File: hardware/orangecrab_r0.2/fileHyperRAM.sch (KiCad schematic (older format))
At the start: 33 parts, among them U4 MT41K64M16TW-107_J-TR

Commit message: hw: Update I/O block routing new DDR3 signals.
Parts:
- gave numbers to parts that had none: 1
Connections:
- net RAM_D0: now also U4.E3 (DQ0); no longer U4.D7 (DQ8)
- net RAM_D1: now also U4.F7 (DQ1); no longer U4.C3 (DQ9)
- net RAM_D10: now also U4.C8 (DQ10); no longer U4.F2 (DQ2)
- net RAM_D11: now also U4.C2 (DQ11); no longer U4.F8 (DQ3)
- net RAM_D12: now also U4.A7 (DQ12); no longer U4.H3 (DQ4)
- net RAM_D13: now also U4.A2 (DQ13); no longer U4.H8 (DQ5)
- net RAM_D14: now also U4.B8 (DQ14); no longer U4.G2 (DQ6)
- net RAM_D15: now also U4.A3 (DQ15); no longer U4.H7 (DQ7)
- net RAM_D2: now also U4.F2 (DQ2); no longer U4.C8 (DQ10)
- net RAM_D3: now also U4.F8 (DQ3); no longer U4.C2 (DQ11)
- net RAM_D4: now also U4.H3 (DQ4); no longer U4.A7 (DQ12)
- net RAM_D5: now also U4.H8 (DQ5); no longer U4.A2 (DQ13)
- net RAM_D6: now also U4.G2 (DQ6); no longer U4.B8 (DQ14)
- net RAM_D7: now also U4.H7 (DQ7); no longer U4.A3 (DQ15)
- net RAM_D8: now also U4.D7 (DQ8); no longer U4.E3 (DQ0)
- net RAM_D9: now also U4.C3 (DQ9); no longer U4.F7 (DQ1)
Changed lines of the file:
@@
 Text GLabel 7050 4100 0    50   Input ~ 0
 RAM_A12
+Text GLabel 8400 3750 2    50   Input ~ 0
+RAM_D0
+Text GLabel 8400 3850 2    50   Input ~ 0
+RAM_D1
+Text GLabel 8400 3950 2    50   Input ~ 0
+RAM_D2
+Text GLabel 8400 4050 2    50   Input ~ 0
+RAM_D3
+Text GLabel 8400 4150 2    50   Input ~ 0
+RAM_D4
+Text GLabel 8400 4250 2    50   Input ~ 0
+RAM_D5
+Text GLabel 8400 4350 2    50   Input ~ 0
+RAM_D6
+Text GLabel 8400 4450 2    50   Input ~ 0
+RAM_D7
 Text GLabel 8400 4650 2    50   Input ~ 0
-RAM_D0
+RAM_D8
 Text GLabel 8400 4750 2    50   Input ~ 0
-RAM_D1
+RAM_D9
 Text GLabel 8400 4850 2    50   Input ~ 0
-RAM_D2
+RAM_D10
 Text GLabel 8400 4950 2    50   Input ~ 0
-RAM_D3
+RAM_D11
 Text GLabel 8400 5050 2    50   Input ~ 0
-RAM_D4
+RAM_D12
 Text GLabel 8400 5150 2    50   Input ~ 0
-RAM_D5
+RAM_D13
 Text GLabel 8400 5250 2    50   Input ~ 0
-RAM_D6
+RAM_D14
 Text GLabel 8400 5350 2    50   Input ~ 0
-RAM_D7
-Text GLabel 8400 3750 2    50   Input ~ 0
-RAM_D8
-Text GLabel 8400 3850 2    50   Input ~ 0
-RAM_D9
-Text GLabel 8400 3950 2    50   Input ~ 0
-RAM_D10
-Text GLabel 8400 4050 2    50   Input ~ 0
-RAM_D11
-Text GLabel 8400 4150 2    50   Input ~ 0
-RAM_D12
-Text GLabel 8400 4250 2    50   Input ~ 0
-RAM_D13
-Text GLabel 8400 4350 2    50   Input ~ 0
-RAM_D14
-Text GLabel 8400 4450 2    50   Input ~ 0
 RAM_D15
 Text GLabel 8400 6000 2    50   Input ~ 0
@@
 RAM_A14
 $Comp
-L Device:R_Pack04 RN?
+L Device:R_Pack04 RN8
 U 1 1 5DE28326
 P 2650 4800
-F 0 "RN?" V 2350 4700 50  0000 C CNN
+F 0 "RN8" V 2350 4700 50  0000 C CNN
 F 1 "50R" V 2350 4950 50  0000 C CNN
 F 2 "Resistor_SMD:R_Array_Convex_4x0402" V 2925 4800 50  0001 C CNN

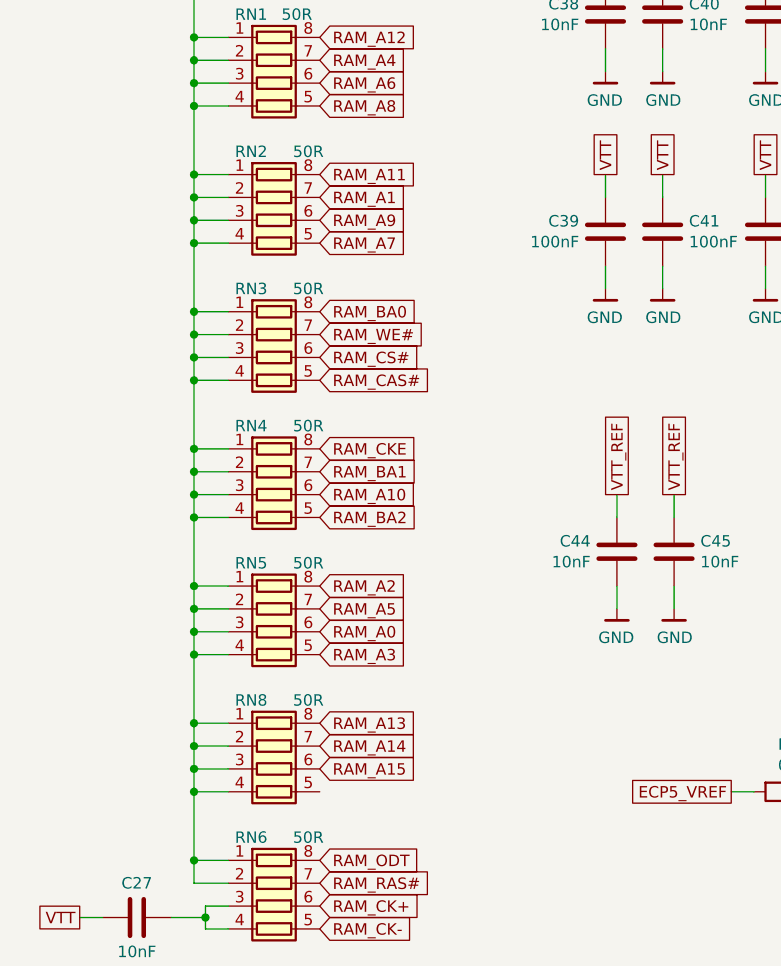
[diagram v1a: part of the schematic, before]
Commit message: hw: update DDR3 signals
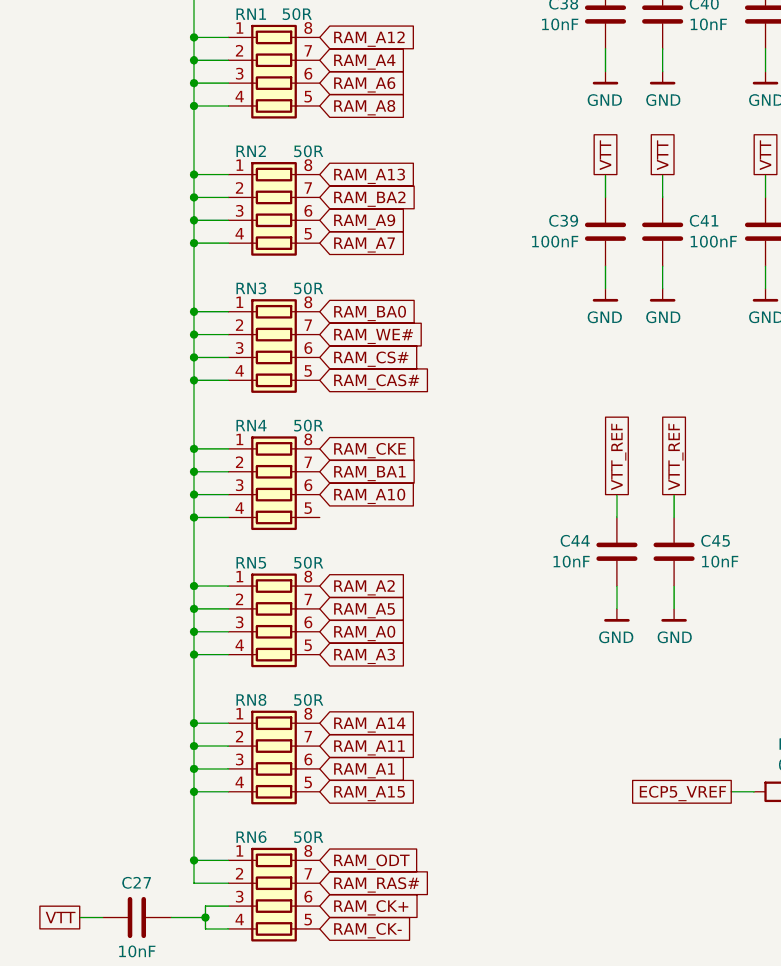
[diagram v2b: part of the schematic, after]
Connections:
- net RAM_A1: now also RN8.6 (R3.2); no longer RN2.7 (R2.2)
- net RAM_A11: now also RN8.7 (R2.2); no longer RN2.8 (R1.2)
- net RAM_A13: now also RN2.8 (R1.2); no longer RN8.8 (R1.2)
- net RAM_A14: now also RN8.8 (R1.2); no longer RN8.7 (R2.2)
- net RAM_A15: now also RN8.5 (R4.2); no longer RN8.6 (R3.2)
- net RAM_BA2: now also RN2.7 (R2.2); no longer RN4.5 (R4.2)
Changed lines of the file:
@@
 Text GLabel 2850 4200 2    50   Input ~ 0
 RAM_A0
-Text GLabel 2850 2300 2    50   Input ~ 0
+Text GLabel 2850 4800 2    50   Input ~ 0
 RAM_A1
 Text GLabel 2850 4000 2    50   Input ~ 0
@@
 Text GLabel 2850 3600 2    50   Input ~ 0
 RAM_A10
-Text GLabel 2850 2200 2    50   Input ~ 0
+Text GLabel 2850 4700 2    50   Input ~ 0
 RAM_A11
 Text GLabel 2850 1600 2    50   Input ~ 0
@@
 Text GLabel 7050 4600 0    50   Input ~ 0
 RAM_BA0
-Text GLabel 2850 3700 2    50   Input ~ 0
+Text GLabel 2850 2300 2    50   Input ~ 0
 RAM_BA2
 Text GLabel 2850 3500 2    50   Input ~ 0
@@
 Text GLabel 7050 4400 0    50   Input ~ 0
 RAM_A15
-Text GLabel 2850 4800 2    50   Input ~ 0
+Text GLabel 2850 4900 2    50   Input ~ 0
 RAM_A15
+Text GLabel 2850 2200 2    50   Input ~ 0
+RAM_A13
 Text GLabel 2850 4600 2    50   Input ~ 0
-RAM_A13
-Text GLabel 2850 4700 2    50   Input ~ 0
 RAM_A14
 $Comp

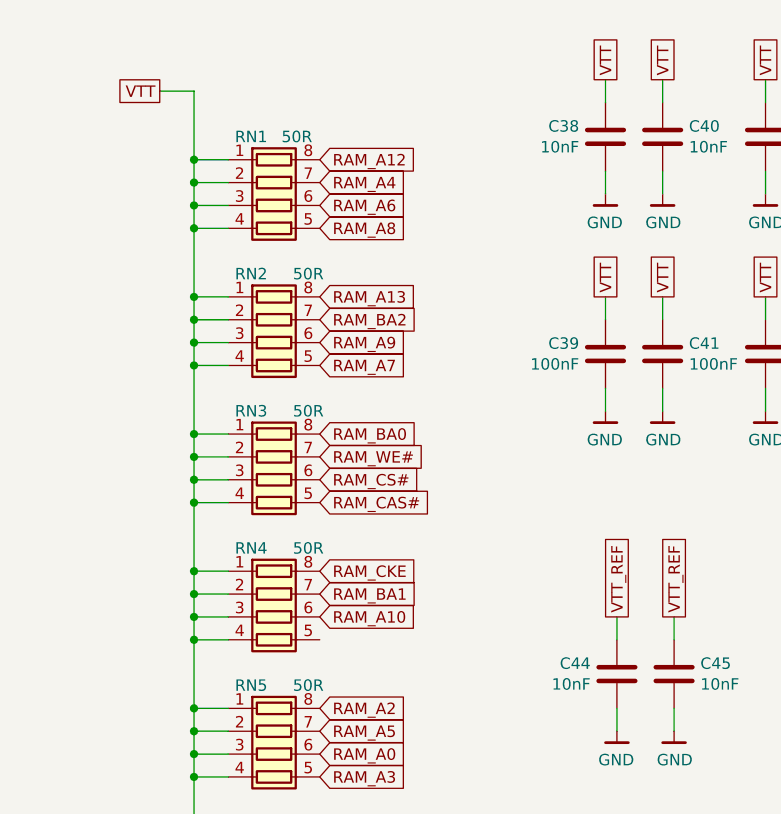
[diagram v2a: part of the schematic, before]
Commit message: hw: Completed first pass of new DD3 routing.
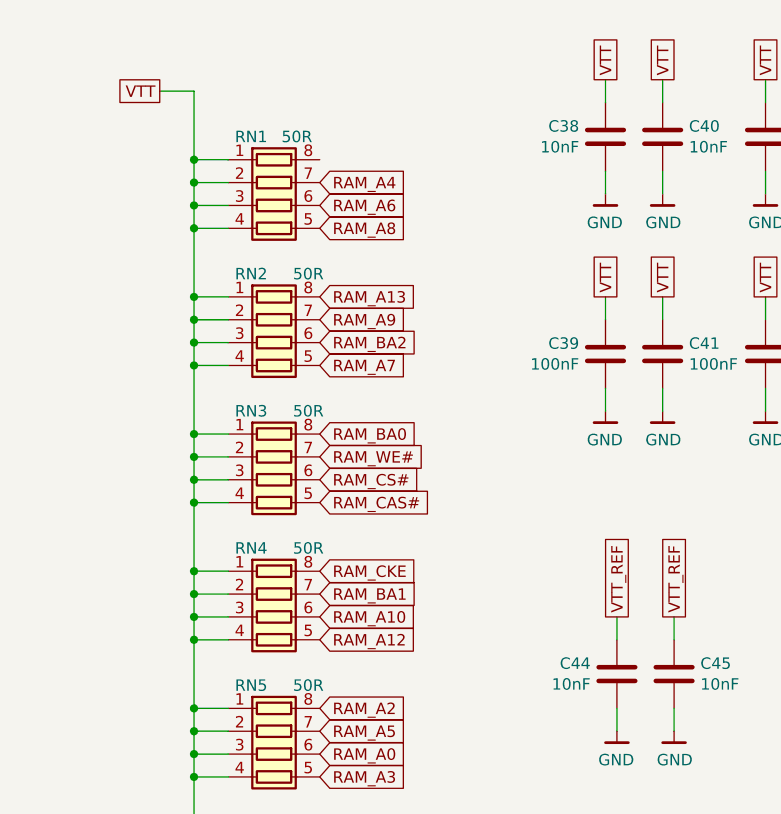
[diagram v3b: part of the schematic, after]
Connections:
- net RAM_A12: now also RN4.5 (R4.2); no longer RN1.8 (R1.2)
- net RAM_A9: now also RN2.7 (R2.2); no longer RN2.6 (R3.2)
- net RAM_BA2: now also RN2.6 (R3.2); no longer RN2.7 (R2.2)
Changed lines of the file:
@@
 Text GLabel 2850 1900 2    50   Input ~ 0
 RAM_A8
-Text GLabel 2850 2400 2    50   Input ~ 0
+Text GLabel 2850 2300 2    50   Input ~ 0
 RAM_A9
 Text GLabel 2850 3600 2    50   Input ~ 0
@@
 Text GLabel 2850 4700 2    50   Input ~ 0
 RAM_A11
-Text GLabel 2850 1600 2    50   Input ~ 0
+Text GLabel 2850 3700 2    50   Input ~ 0
 RAM_A12
 Text GLabel 10450 1950 2    50   UnSpc ~ 0
@@
 Text GLabel 7050 4600 0    50   Input ~ 0
 RAM_BA0
-Text GLabel 2850 2300 2    50   Input ~ 0
+Text GLabel 2850 2400 2    50   Input ~ 0
 RAM_BA2
 Text GLabel 2850 3500 2    50   Input ~ 0

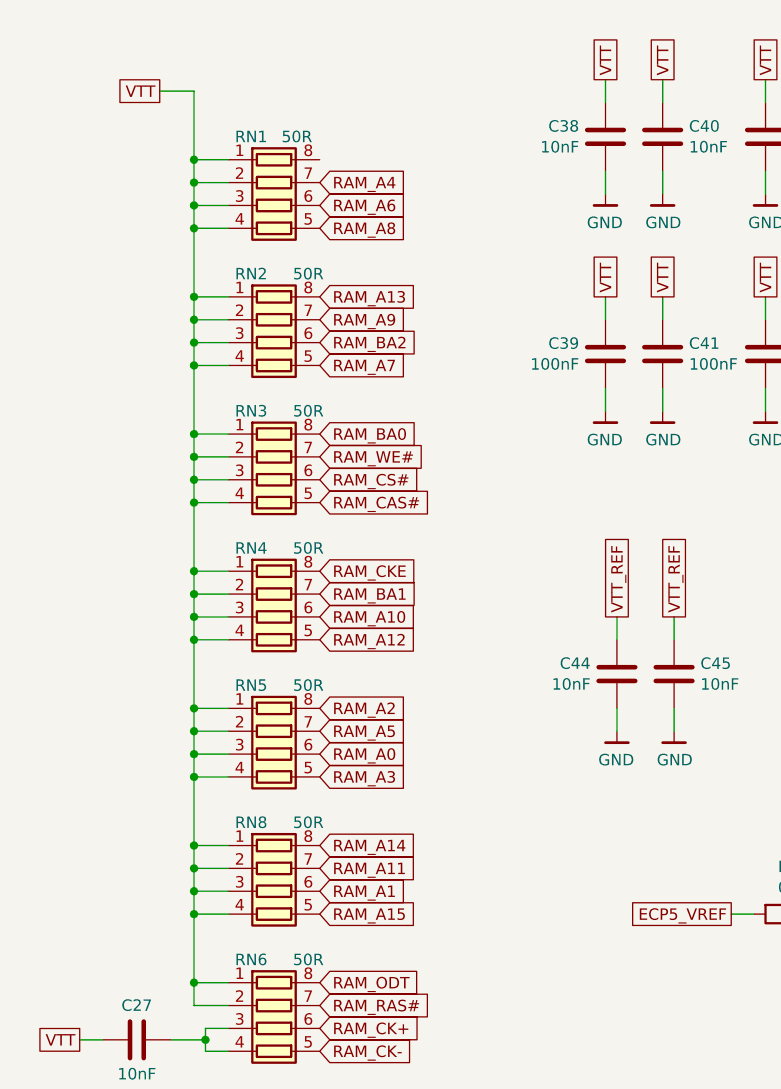
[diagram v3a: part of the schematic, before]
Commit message: hw: Update microSD card
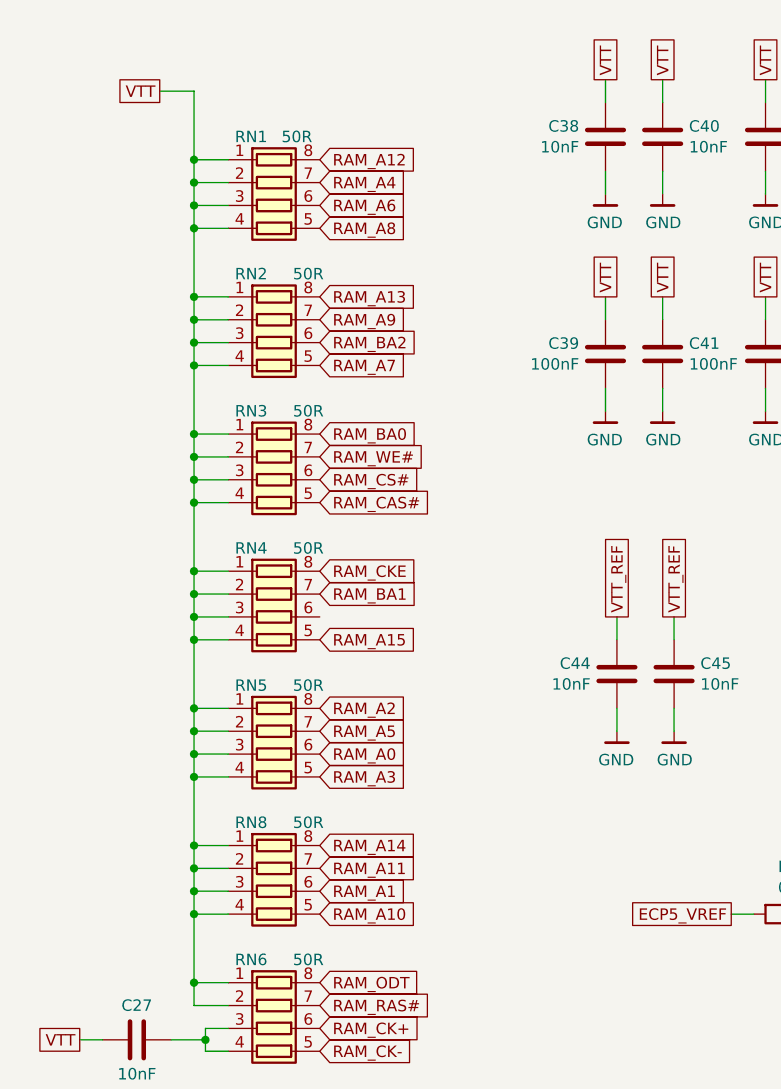
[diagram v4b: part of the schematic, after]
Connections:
- net RAM_A10: now also RN8.5 (R4.2); no longer RN4.6 (R3.2)
- net RAM_A12: now also RN1.8 (R1.2); no longer RN4.5 (R4.2)
- net RAM_A15: now also RN4.5 (R4.2); no longer RN8.5 (R4.2)
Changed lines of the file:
@@
 Text GLabel 2850 2300 2    50   Input ~ 0
 RAM_A9
-Text GLabel 2850 3600 2    50   Input ~ 0
+Text GLabel 2850 4900 2    50   Input ~ 0
 RAM_A10
 Text GLabel 2850 4700 2    50   Input ~ 0
 RAM_A11
-Text GLabel 2850 3700 2    50   Input ~ 0
+Text GLabel 2850 1600 2    50   Input ~ 0
 RAM_A12
 Text GLabel 10450 1950 2    50   UnSpc ~ 0
@@
 Text GLabel 7050 4400 0    50   Input ~ 0
 RAM_A15
-Text GLabel 2850 4900 2    50   Input ~ 0
+Text GLabel 2850 3700 2    50   Input ~ 0
 RAM_A15
 Text GLabel 2850 2200 2    50   Input ~ 0

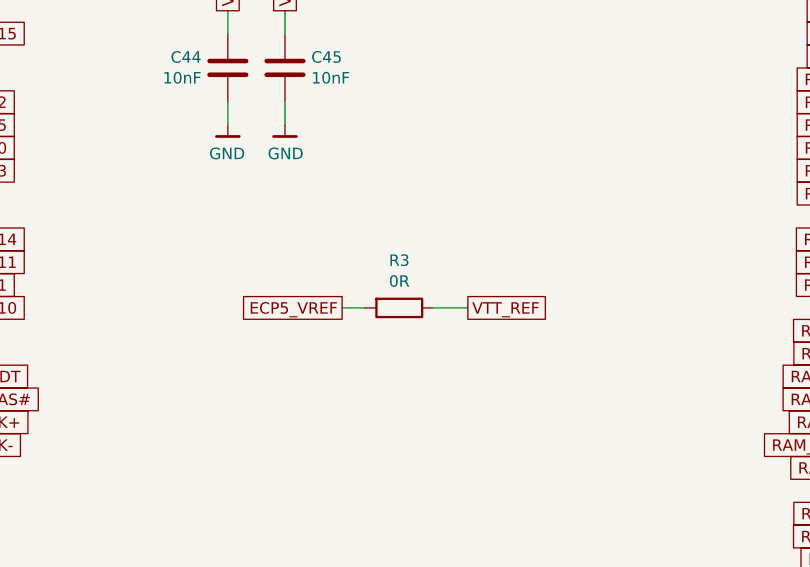
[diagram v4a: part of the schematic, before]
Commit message: hw: Update board with 3d models Finish pin-swaps and routing of open changes General cleanups
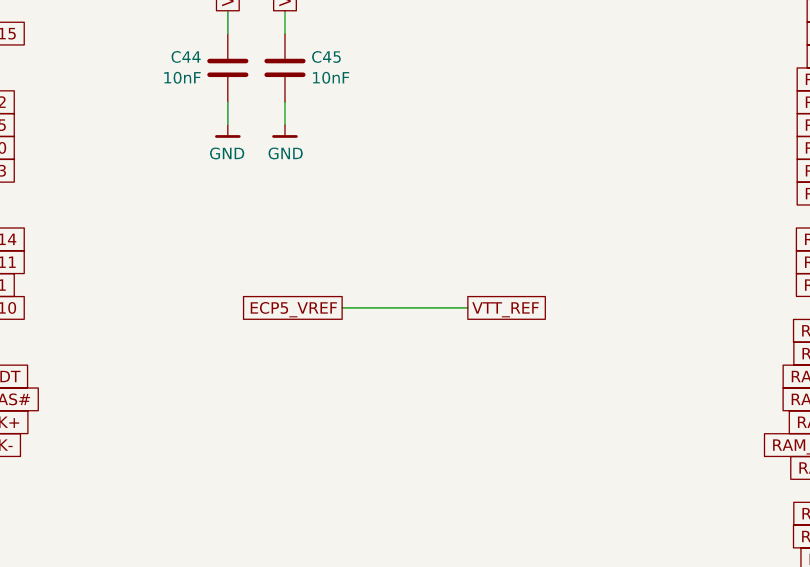
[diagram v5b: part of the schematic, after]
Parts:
- removed R3: 0R, Resistor_SMD:R_0201_0603Metric, symbol Device:R
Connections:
- net VTT_REF is gone; now on net ECP5_VREF: C44.2, C45.2, U4.H1 (VREFDQ), U4.M8 (VREFCA)
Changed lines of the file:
@@
 Text GLabel 5200 4900 2    50   UnSpc ~ 0
 VTT_REF
-$Comp
-L Device:R R3
-U 1 1 5D601972
-P 4900 4900
-F 0 "R3" V 4693 4900 50  0000 C CNN
-F 1 "0R" V 4784 4900 50  0000 C CNN
-F 2 "Resistor_SMD:R_0201_0603Metric" V 4830 4900 50  0001 C CNN
-F 3 "~" H 4900 4900 50  0001 C CNN
-F 4 "‎Yageo‎" H 4900 4900 50  0001 C CNN "Mfg"
-F 5 "RC0201FR-070RL" H 4900 4900 50  0001 C CNN "PN"
-	1    4900 4900
-	0    1    1    0
-$EndComp
-Wire Wire Line
-	4650 4900 4750 4900
-Wire Wire Line
-	5050 4900 5200 4900
 Text GLabel 7050 4200 0    50   Input ~ 0
 RAM_A13
@@
 Wire Wire Line
 	2300 4900 2300 4800
+Wire Wire Line
+	4650 4900 5200 4900
 $EndSCHEMATC
